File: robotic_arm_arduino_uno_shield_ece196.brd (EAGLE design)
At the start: 44.5 x 53.3 mm, 34 parts, among them J1 (ID,OD)=(2.1,5.5)MM, J2 1x06-VERT-MALE, J3 1x06-VERT-MALE, J4 1x08-VERT-MALE, J5 1x08-VERT-MALE

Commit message: Fix inconsistency
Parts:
- removed C83, C98: 0.1uF/50V, MrSwirlyEyes:CAP_CER_SMD-805
- removed C94, C97: 10uF/25V, MrSwirlyEyes:CAP_CER_SMD-805
- removed D7: 1A/50V, MrSwirlyEyes:DIODE_SMD_1A-50V-SOD123F
- removed VREG3: 5A/5V, MrSwirlyEyes:TO-263-5
- added C2: 0.22uF/50V, MrSwirlyEyes:CAP_CER_SMD-805
- added C3, C4: 0.1uF/50V, MrSwirlyEyes:CAP_CER_SMD-805
- added C5, C6: 100UF/16V, MrSwirlyEyes:CAP_POL_SMD_L6.6-W6.6
- added D4, D5: 1A/50V, MrSwirlyEyes:DIODE_SMD_1A-50V-SOD123F
- added VREG1, VREG2: 1.5A/5V, MrSwirlyEyes:SOT223
- C1: value 100UF/16V -> 0.22uF/50V; device MrSwirlyEyes:CAP_POL_SMD_L6.6-W6.6 -> MrSwirlyEyes:CAP_CER_SMD-805
- R0, R1, R2, R3, R4: device MrSwirlyEyes:RESISTOR_SMD-805 -> MrSwirlyEyes:RESC2012X60_HS
- moved C1 18.4 mm to (25.4, 25.4), turned to 180 degrees
- moved REC_LED 9.67 mm to (-7.62, 19.1)
- moved SERVO4 9.14 mm to (17.5, 45.2)
- moved R3 8.98 mm to (-3.17, 19.1)
- moved PLAY_LED 8.89 mm to (-7.62, 29.2)
- moved R1 8.52 mm to (0.00, 19.1)
- moved R4 8.13 mm to (-3.17, 29.2)
- moved S2 7.79 mm to (-1.27, 7.87)
- moved R2 7.62 mm to (0.00, 29.2)
- moved S3 7.44 mm to (-1.27, 40.6)
- moved C0 3.18 mm to (35.6, 30.5), turned to 0 degrees
- moved SUPPLY14 2.62 mm to (36.8, 17.3)
- moved LIPO 2.59 mm to (44.5, 30.5)
- moved J1 2.54 mm to (39.4, 19.1)
- moved POT1 2.54 mm to (29.2, 8.13)
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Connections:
- removed net VCC: C1.A, C83.1, C94.1, D7.A, SERVO1.2, SERVO2.2, SERVO3.2, SERVO4.2, VREG3.4
- new net VCC_1: C3.1, C5.A, D5.A, SERVO1.2, SERVO2.2, VREG1.3
- new net VCC_2: C4.1, C6.A, D4.A, SERVO3.2, SERVO4.2, VREG2.3
- net GND: now also C1.2, C2.2, C3.2, C4.2, C5.K, C6.K, VREG1.2, VREG1.4, VREG2.2, VREG2.4; no longer C97.2, C98.2
- net NGND: no longer C1.K, C83.2, C94.2, VREG3.3, VREG3.TAB
- net VIN: now also C1.1, C2.1, D4.K, D5.K, VREG1.1, VREG2.1; no longer C97.1, C98.1, D7.K, VREG3.1, VREG3.2
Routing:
- net NGND: track 93.2 -> 15.2 mm, vias 29 -> 0
- net D10: track 38.3 -> 50.4 mm
- net D7: track 66.9 -> 78.4 mm
- net GND: track 6.63 -> 17.3 mm, vias 3 -> 8
- net VIN: track 36.3 -> 44.9 mm
- net VCC: track 7.62 -> 0.00 mm
- net D9: track 10.4 -> 3.05 mm
- net D8: track 45.0 -> 51.5 mm, vias 1 -> 0
- net D11: track 25.0 -> 30.9 mm
- net 5V: track 75.2 -> 71.6 mm
- net N$4: track 2.63 -> 3.82 mm
- net D6: track 4.10 -> 3.05 mm
- net D5: track 4.10 -> 3.05 mm
- net A3: track 4.10 -> 3.05 mm
- net A2: track 4.10 -> 3.05 mm
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- added copper zone on layer 1, net VCC_1
- added copper zone on layer 1, net VCC_2
- removed copper zone on layer 16, net +
- removed copper zone on layer 1, net -
- removed copper zone on layer 1, net NGND
- removed copper zone on layer 1, net VCC
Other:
- board size 44.5 x 53.3 mm -> 55.9 x 53.3 mm
- board text added: "1A/50V"
- board text added: "Rev 2"
- board text added: "Rev 2 Designed by: Buu Truong CADed by: MrSwirlyEyes"
- board text removed: "Rev 3"
- board text removed: "Rev 3 Designed by: Buu Truong CADed by: MrSwirlyEyes"

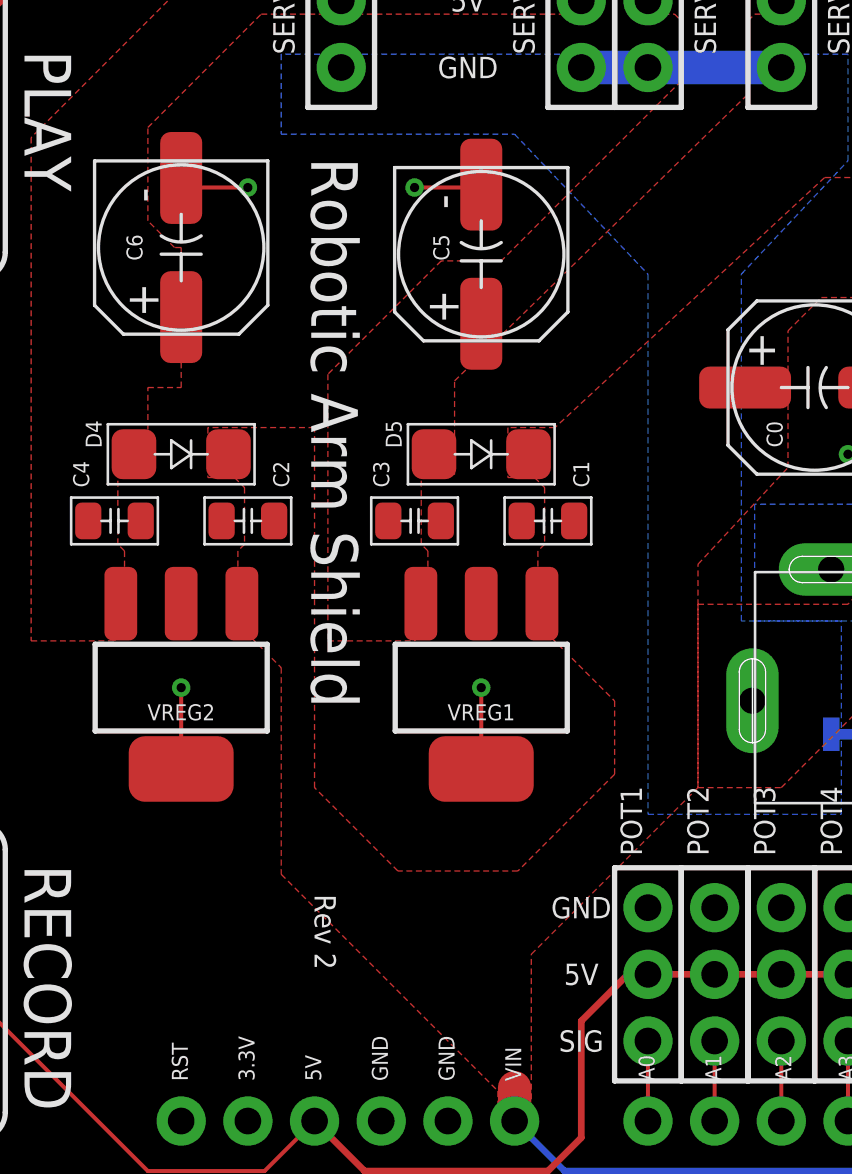
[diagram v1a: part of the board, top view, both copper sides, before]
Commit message: Rev 3: ECE 196 board.  Add PiB logo.
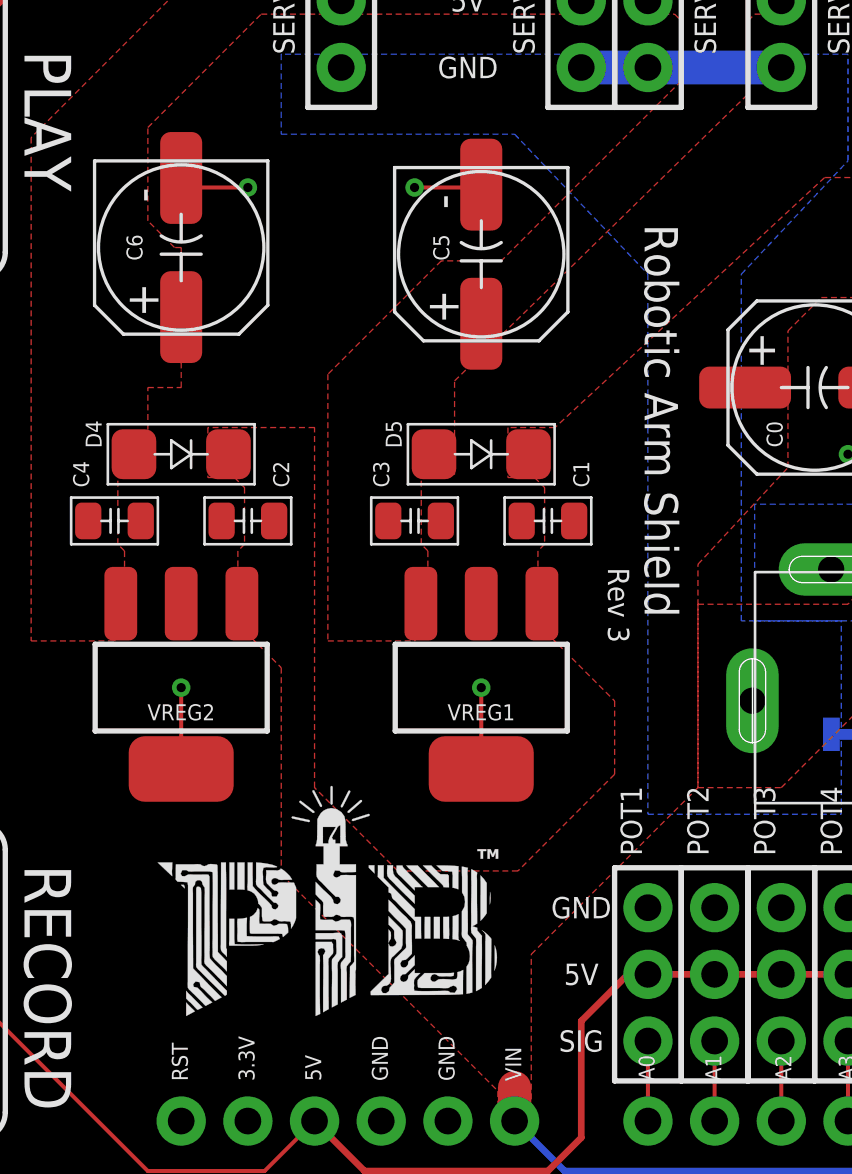
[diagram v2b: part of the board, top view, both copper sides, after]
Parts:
- added U$1, U$3: (no value), PiB_logo:PIB-LOGO
- added U$2: (no value), PiB_logo:MRSWIRLYEYES-LOGO
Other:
- board text added: "Rev 3"
- board text added: "Rev 3 Designed by: Buu Truong CADed by: MrSwirlyEyes"
- board text removed: "Rev 2"
- board text removed: "Rev 2 Designed by: Buu Truong CADed by: MrSwirlyEyes"
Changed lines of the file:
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@@
 <?xml version="1.0" encoding="utf-8"?>
 <!DOCTYPE eagle SYSTEM "eagle.dtd">
-<eagle version="8.3.1">
+<eagle version="8.7.1">
 <drawing>
 <settings>
@@
 <layer number="59" name="tCarbon" color="7" fill="1" visible="no" active="no"/>
 <layer number="60" name="bCarbon" color="7" fill="1" visible="no" active="no"/>
+<layer number="88" name="SimResults" color="9" fill="1" visible="no" active="no"/>
+<layer number="89" name="SimProbes" color="9" fill="1" visible="no" active="no"/>
 <layer number="90" name="Modules" color="5" fill="1" visible="no" active="no"/>
 <layer number="91" name="Nets" color="2" fill="1" visible="no" active="no"/>
@@
 <text x="44.323" y="13.589" size="0.6096" layer="21" font="vector" ratio="10" align="center">7.4V-12V</text>
 <text x="42.164" y="30.353" size="0.6096" layer="21" font="vector" ratio="10" rot="R90" align="center">7.4V-12V</text>
-<text x="16.383" y="39.243" size="1.778" layer="21" font="vector" ratio="20" rot="SR270">Robotic Arm Shield</text>
-<text x="16.51" y="11.176" size="0.8128" layer="21" font="vector" ratio="10" rot="SR270">Rev 2</text>
-<text x="24.13" y="10.16" size="1.778" layer="22" font="vector" ratio="20" rot="MR0">Robotic Arm Shield</text>
-<text x="24.13" y="9.525" size="0.8128" layer="22" font="vector" ratio="10" rot="MR0" align="top-left">Rev 2
+<text x="29.083" y="36.703" size="1.27" layer="21" font="vector" ratio="20" rot="SR270">Robotic Arm Shield</text>
+<text x="27.686" y="23.622" size="0.8128" layer="21" font="vector" ratio="10" rot="SR270">Rev 3</text>
+<text x="16.51" y="36.83" size="1.778" layer="22" font="vector" ratio="20" rot="SMR270">Robotic Arm Shield</text>
+<text x="17.145" y="36.83" size="0.8128" layer="22" font="vector" ratio="10" rot="SMR270" align="top-left">Rev 3
 Designed by: Buu Truong
 CADed by: MrSwirlyEyes</text>
@@
 <param name="dpMaxLengthDifference" value="10mm"/>
 <param name="dpGapFactor" value="2.5"/>
-<param name="checkGrid" value="0"/>
 <param name="checkAngle" value="0"/>
 <param name="checkFont" value="1"/>
 <param name="checkRestrict" value="1"/>
+<param name="checkStop" value="0"/>
+<param name="checkValues" value="0"/>
 <param name="useDiameter" value="13"/>
 <param name="maxErrors" value="50"/>
@@
 <attribute name="VALUE" x="29.718" y="13.716" size="0.6096" layer="27" font="vector" ratio="10" rot="R90" align="center"/>
 </element>
+<element name="U$1" library="PiB_logo" package="PIB-LOGO" value="" x="6.35" y="26.67" rot="MR270"/>
+<element name="U$2" library="PiB_logo" package="MRSWIRLYEYES-LOGO" value="" x="26.67" y="27.94" rot="MR270"/>
+<element name="U$3" library="PiB_logo" package="PIB-LOGO" value="" x="17.018" y="10.922"/>
 </elements>
 <signals>

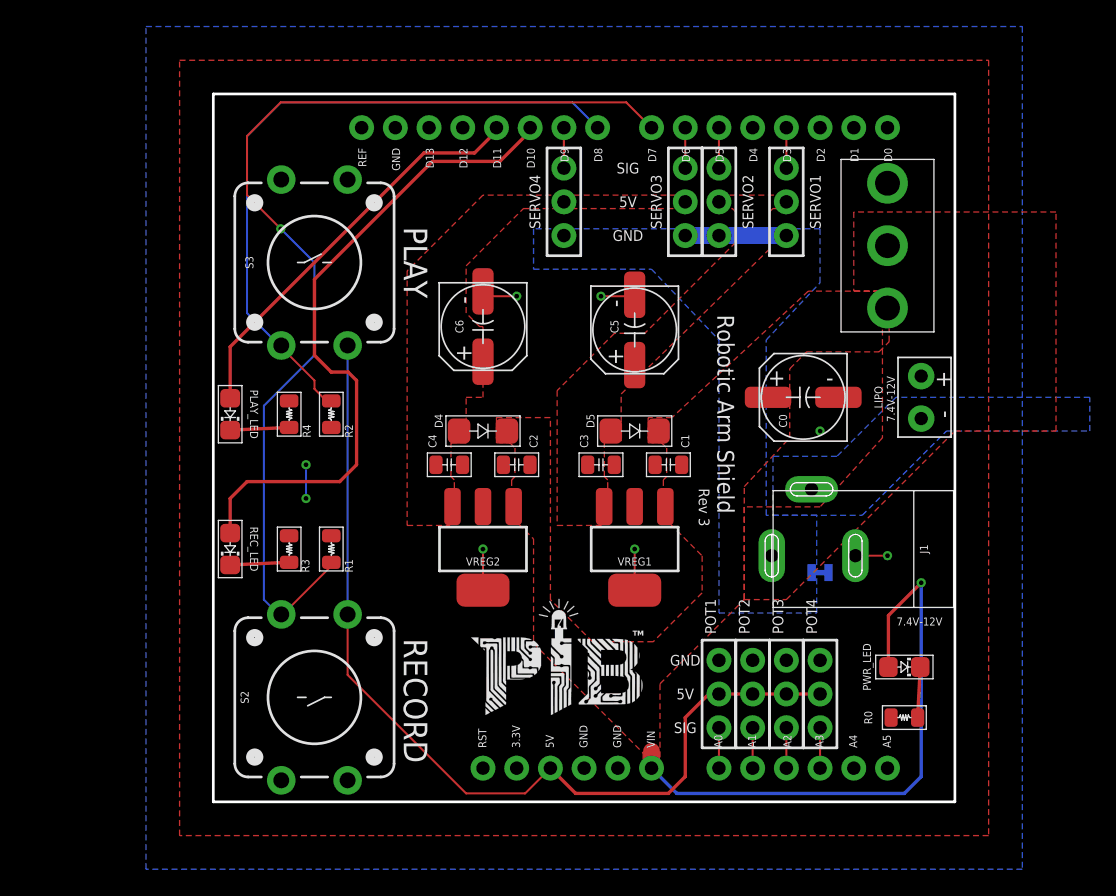
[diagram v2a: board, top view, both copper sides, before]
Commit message: Updated ECE196 board.  Made a bit smaller
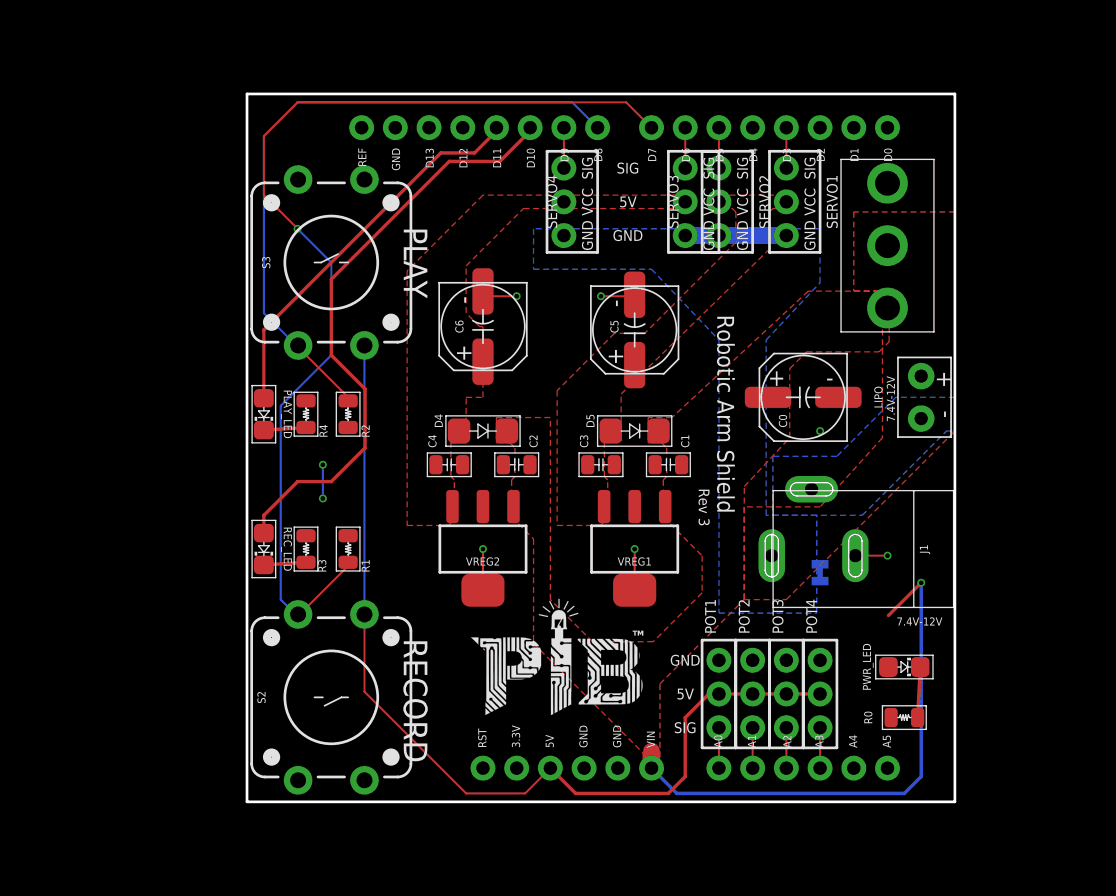
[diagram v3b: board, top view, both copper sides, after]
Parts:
- C0, C5, C6: device MrSwirlyEyes:CAP_POL_SMD_L6.6-W6.6 -> PiB_capacitors:_AE_SMD_L6.6-W6.6
- C1, C2, C3, C4: device MrSwirlyEyes:CAP_CER_SMD-805 -> PiB_capacitors:_CER_SMD-805
- D4, D5: device MrSwirlyEyes:DIODE_SMD_1A-50V-SOD123F -> PiB_discrete_semiconductors:SOD123F
- J1: device MrSwirlyEyes:POWER_JACK_SLOT_ID2.1MM-OD5.5MM -> PiB_connectors:POWER_JACK_SLOT_ID2.1MM-OD5.5MM
- J2, J3: value 1x06-VERT-MALE -> 1x06-VERT-FEMALE; device connectors:1X06-VERT-MALE -> PiB_connectors:1X06-VERT-FEMALE
- J4, J5: value 1x08-VERT-MALE -> 1x08-VERT-FEMALE; device connectors:1X08-VERT-MALE -> PiB_connectors:1X08-VERT-FEMALE
- LIPO: value BATTERYPTH_HOLES -> 7.4V; device MrSwirlyEyes:DUAL_PTH_PADS -> PiB_batteries:DUAL_PTH_PADS
- PLAY_LED, PWR_LED, REC_LED: device MrSwirlyEyes:LED_SMD-805_ -> PiB_leds:LED_SMD-805_
- POT1, POT2, POT3, POT4: value 20KΩ -> 10KΩ; device MrSwirlyEyes:CONNECTOR_POTENTIOMETER_NO-MARKINGS_FEMALE-HEADER -> PiB_resistors:CONNECTOR_POTENTIOMETER_NO-MARKINGS_FEMALE-HEADER
- R0, R1, R2, R4: device MrSwirlyEyes:RESC2012X60_HS -> PiB_resistors:RESISTOR_SMD-805
- R3: value 2KΩ -> 1KΩ; device MrSwirlyEyes:RESC2012X60_HS -> PiB_resistors:RESISTOR_SMD-805
- S1: device MrSwirlyEyes:SW-SLIDE_SPDT_5A-28V_13L-7W -> PiB_switches:SW_TOGGLE_SPDT_5A-28V_13L-7W
- S2, S3: device MrSwirlyEyes:SPST-PTH-12MM -> PiB_switches:BTN_MOMENTARY_SPST-NO_PTH_L12-W12
- SERVO1, SERVO2, SERVO3, SERVO4: device MrSwirlyEyes:CONNECTOR_SERVO_NO-MARKINGS -> PiB:CONNECTOR_SERVO
- SUPPLY14: device SparkFun-PowerSymbols:2PT_GND_TIE -> PiB_power_symbols:2PT_GND_TIE
- VREG1, VREG2: value 1.5A/5V -> LM340MP-5 1.5A/5V; device MrSwirlyEyes:SOT223 -> PiB_ic_power:SOT223-4
- moved PLAY_LED 2.54 mm to (-5.08, 29.2)
- moved REC_LED 2.54 mm to (-5.08, 19.1)
- moved SERVO1 1.27 mm to (35.6, 45.2)
- moved R1 1.27 mm to (1.27, 19.1)
- moved R2 1.27 mm to (1.27, 29.2)
- moved S2 1.27 mm to (0.00, 7.87)
- moved S3 1.27 mm to (0.00, 40.6)
- moved R3 1.27 mm to (-1.91, 19.1)
- moved R4 1.27 mm to (-1.91, 29.2)
- moved SERVO2 1.27 mm to (30.5, 45.2)
- moved SERVO3 1.27 mm to (27.9, 45.2)
- moved SERVO4 1.27 mm to (18.8, 45.2)
- turned S1 to 180 degrees
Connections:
- new net VCC: C0.A, C1.1, C2.1, D4.K, D5.K, PWR_LED.A, S1.1, VREG1.1, VREG2.1
- net +: now also S1.2; no longer S1.P$2
- net GND: now also VREG1.TAB, VREG2.TAB; no longer VREG1.4, VREG2.4
- net VIN: no longer C0.A, C1.1, C2.1, D4.K, D5.K, PWR_LED.A, S1.P$1, VREG1.1, VREG2.1
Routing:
- net D10: track 50.4 -> 44.7 mm
- net VIN: track 44.9 -> 41.0 mm
- net D11: track 30.9 -> 29.1 mm
- net D7: track 78.4 -> 77.1 mm
- net N$2: track 4.45 -> 3.18 mm
- net N$1: track 4.45 -> 3.18 mm
- net D8: track 51.5 -> 50.5 mm
- net 5V: track 71.6 -> 71.1 mm
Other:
- board size 55.9 x 53.3 mm -> 53.3 x 53.3 mm

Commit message: Small corrections.
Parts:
- removed J2, J3: 1x06-VERT-FEMALE, PiB_connectors:1X06-VERT-FEMALE
- removed J4, J5: 1x08-VERT-FEMALE, PiB_connectors:1X08-VERT-FEMALE
- added ARDUINO1: Arduino UNO R3, PiB_boards:ARDUINO_UNO_R3_NO-HOLES_NO-AVR-ISP_NO-I2C_NO-NC_NO-IOREF
- J1: device PiB_connectors:POWER_JACK_SLOT_ID2.1MM-OD5.5MM -> PiB_connectors:POWER_JACK_PTH_ID2.1MM-OD5.5MM
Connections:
- removed net A4: J3.2
- removed net A5: J3.1
- removed net VCC: C0.A, C1.1, C2.1, D4.K, D5.K, PWR_LED.A, S1.1, VREG1.1, VREG2.1
- new net N$29: ARDUINO1.A0
- new net N$30: ARDUINO1.A1
- new net N$31: ARDUINO1.A2
- new net N$32: ARDUINO1.A3
- new net N$33: ARDUINO1.A4
- new net N$34: ARDUINO1.A5
- net 3.3V: now also ARDUINO1.3.3V; no longer J2.2
- net 5V: now also ARDUINO1.5V; no longer J2.3
- net A0: no longer J3.6
- net A1: no longer J3.5
- net A2: no longer J3.4
- net A3: no longer J3.3
- net AREF: now also ARDUINO1.AREF; no longer J5.8
- net D10: now also ARDUINO1.D10; no longer J5.3
- net D11: now also ARDUINO1.D11; no longer J5.4
- net D12: now also ARDUINO1.D12; no longer J5.5
- net D13: now also ARDUINO1.D13; no longer J5.6
- net D2: now also ARDUINO1.D2; no longer J4.3
- net D3: now also ARDUINO1.D3; no longer J4.4
- net D4: now also ARDUINO1.D4; no longer J4.5
- net D5: now also ARDUINO1.D5; no longer J4.6
- net D6: now also ARDUINO1.D6; no longer J4.7
- net D7: now also ARDUINO1.D7; no longer J4.8
- net D8: now also ARDUINO1.D8; no longer J5.1
- net D9: now also ARDUINO1.D9; no longer J5.2
- net GND: now also ARDUINO1.GND@1, ARDUINO1.GND@2, ARDUINO1.GND@3; no longer J2.4, J2.5, J5.7
- net RESET: now also ARDUINO1.RESET@1; no longer J2.1
- net RX: now also ARDUINO1.D0; no longer J4.1
- net TX: now also ARDUINO1.D1; no longer J4.2
- net VIN: now also ARDUINO1.VIN, C0.A, C1.1, C2.1, D4.K, D5.K, PWR_LED.A, S1.1, VREG1.1, VREG2.1; no longer J2.6
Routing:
- net A3: track 3.05 -> 0.00 mm
- net A2: track 3.05 -> 0.00 mm
- net A1: track 3.05 -> 0.00 mm
- net A0: track 3.05 -> 0.00 mm
- net VIN: track 41.0 -> 43.6 mm
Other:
- board text added: "Rev 4"
- board text added: "Rev 4 Designed by: Buu Truong CADed by: MrSwirlyEyes"
- board text removed: "Rev 3"
- board text removed: "Rev 3 Designed by: Buu Truong CADed by: MrSwirlyEyes"
